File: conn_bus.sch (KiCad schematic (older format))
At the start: 1 part, among them J3 Conn_02x08_Odd_Even

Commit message: program counter
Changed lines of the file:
@@
 EESchema Schematic File Version 4
-LIBS:alu_pcb-cache
+LIBS:program_counter_pcb-cache
 EELAYER 30 0
 EELAYER END
 $Descr A4 11693 8268
 encoding utf-8
-Sheet 6 10
+Sheet 6 6
 Title ""
 Date ""
@@
 AR Path="/5EE5702D/5EF022DA" Ref="J3"  Part="1"
 AR Path="/5EE573A3/5EF022DA" Ref="J4"  Part="1"
-F 0 "J6" H 4350 2842 50  0000 C CNN
+AR Path="/5EF3E141/5EF022DA" Ref="J3"  Part="1"
+F 0 "J3" H 4350 2842 50  0000 C CNN
 F 1 "Conn_02x08_Odd_Even" H 4350 2751 50  0000 C CNN
 F 2 "Connector_PinHeader_2.54mm:PinHeader_2x08_P2.54mm_Vertical" H 4300 2325 50  0001 C CNN

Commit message: way to long since last commit
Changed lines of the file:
@@
 EESchema Schematic File Version 4
-LIBS:program_counter_pcb-cache
 EELAYER 30 0
 EELAYER END
 $Descr A4 11693 8268
 encoding utf-8
-Sheet 6 6
+Sheet 10 13
 Title ""
 Date ""
@@
 AR Path="/5EE573A3/5EF022DA" Ref="J4"  Part="1"
 AR Path="/5EF3E141/5EF022DA" Ref="J3"  Part="1"
-F 0 "J3" H 4350 2842 50  0000 C CNN
+AR Path="/5F1B2824/5EF022DA" Ref="J2"  Part="1"
+AR Path="/5F1826BB/5EF022DA" Ref="J3"  Part="1"
+AR Path="/5F6449BD/5EF022DA" Ref="J2"  Part="1"
+AR Path="/5F644FEB/5EF022DA" Ref="J3"  Part="1"
+AR Path="/5F64572D/5EF022DA" Ref="J4"  Part="1"
+F 0 "J2" H 4350 2842 50  0000 C CNN
 F 1 "Conn_02x08_Odd_Even" H 4350 2751 50  0000 C CNN
 F 2 "Connector_PinHeader_2.54mm:PinHeader_2x08_P2.54mm_Vertical" H 4300 2325 50  0001 C CNN

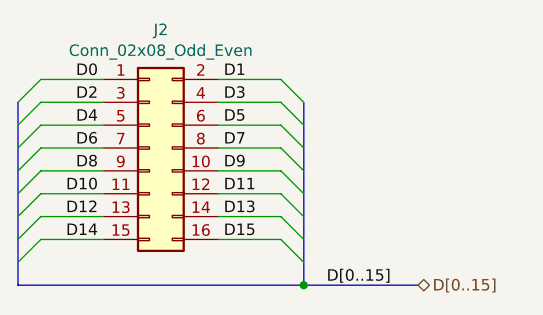
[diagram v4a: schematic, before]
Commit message: memory programmer and cu
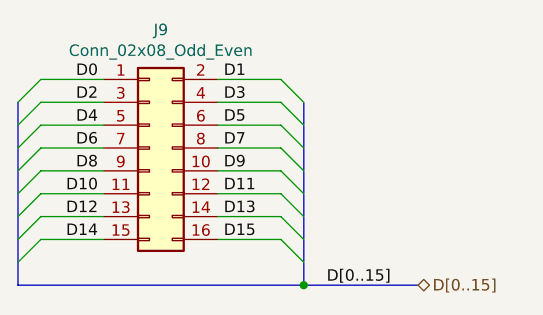
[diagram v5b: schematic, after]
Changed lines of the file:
@@
 EESchema Schematic File Version 4
-LIBS:buttons_pcb-cache
+LIBS:control_unit_pcb-cache
 EELAYER 30 0
 EELAYER END
 $Descr A4 11693 8268
 encoding utf-8
-Sheet 5 5
+Sheet 10 10
 Title ""
 Date ""
@@
 AR Path="/5F64572D/5EF022DA" Ref="J4"  Part="1"
 AR Path="/5F408B3F/5EF022DA" Ref="J2"  Part="1"
-F 0 "J2" H 4350 2842 50  0000 C CNN
+AR Path="/5F532AEF/5EF022DA" Ref="J8"  Part="1"
+AR Path="/5F532D3A/5EF022DA" Ref="J9"  Part="1"
+F 0 "J9" H 4350 2842 50  0000 C CNN
 F 1 "Conn_02x08_Odd_Even" H 4350 2751 50  0000 C CNN
 F 2 "Connector_PinHeader_2.54mm:PinHeader_2x08_P2.54mm_Vertical" H 4300 2325 50  0001 C CNN

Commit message: connect cu and start creating material csv
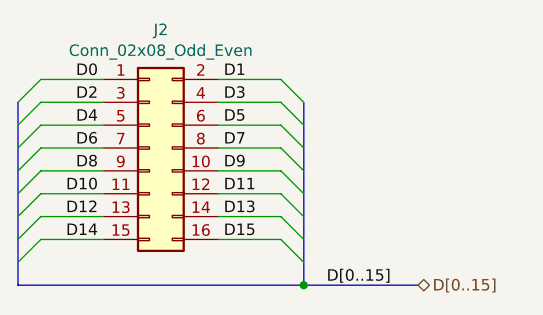
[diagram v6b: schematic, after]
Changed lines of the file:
@@
 EESchema Schematic File Version 4
-LIBS:control_unit_pcb-cache
+LIBS:bit_shifter_pcb-cache
 EELAYER 30 0
 EELAYER END
 $Descr A4 11693 8268
 encoding utf-8
-Sheet 10 10
+Sheet 5 6
 Title ""
 Date ""
@@
 AR Path="/5F532AEF/5EF022DA" Ref="J8"  Part="1"
 AR Path="/5F532D3A/5EF022DA" Ref="J9"  Part="1"
-F 0 "J9" H 4350 2842 50  0000 C CNN
+F 0 "J2" H 4350 2842 50  0000 C CNN
 F 1 "Conn_02x08_Odd_Even" H 4350 2751 50  0000 C CNN
 F 2 "Connector_PinHeader_2.54mm:PinHeader_2x08_P2.54mm_Vertical" H 4300 2325 50  0001 C CNN

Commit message: part lists
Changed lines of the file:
@@
 EESchema Schematic File Version 4
-LIBS:bit_shifter_pcb-cache
+LIBS:program_counter_pcb-cache
 EELAYER 30 0
 EELAYER END
@@
 AR Path="/5F532AEF/5EF022DA" Ref="J8"  Part="1"
 AR Path="/5F532D3A/5EF022DA" Ref="J9"  Part="1"
-F 0 "J2" H 4350 2842 50  0000 C CNN
+F 0 "J3" H 4350 2842 50  0000 C CNN
 F 1 "Conn_02x08_Odd_Even" H 4350 2751 50  0000 C CNN
 F 2 "Connector_PinHeader_2.54mm:PinHeader_2x08_P2.54mm_Vertical" H 4300 2325 50  0001 C CNN
